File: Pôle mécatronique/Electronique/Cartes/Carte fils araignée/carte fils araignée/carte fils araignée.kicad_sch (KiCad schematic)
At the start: 17 parts, among them J1 Conn_01x05, J10 Conn_01x05, J11 Conn_01x05, J12 Conn_01x05, J13 Conn_01x05, J2 Conn_01x05, J3 Conn_01x05, J4 Conn_01x05, J5 Conn_01x03, J6 Conn_01x03, J7 Conn_01x05, J8 Conn_01x03, J9 Conn_01x04

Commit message: Update Araignée & Odométrie
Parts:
- J5: value Conn_01x03 -> X3
- J6: value Conn_01x03 -> X1
- J8: value Conn_01x03 -> X2
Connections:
- net Xshut5: now also J6.1 (Pin_1); no longer J6.2 (Pin_2)
- net Xshut6: now also J6.2 (Pin_2); no longer J6.1 (Pin_1)
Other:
- moved on the sheet: J5, J6, J8

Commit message: Panique totale
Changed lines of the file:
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@@
     (pin "4")
+  )
+  (symbol (lib_id "Graphic:Logo_Open_Hardware_Small") (at 238.76 48.26 0) (unit 1)
+    (in_bom yes) (on_board yes)
+    (property "Reference" "#LOGO1" (id 0) (at 238.76 41.275 0)
+      (effects (font (size 1.27 1.27)) hide)
+    )
+    (property "Value" "Logo_Open_Hardware_Small" (id 1) (at 238.76 53.975 0)
+      (effects (font (size 1.27 1.27)) hide)
+    )
+    (property "Footprint" "Logos:logoRobotechNancy10x10" (id 2) (at 238.76 48.26 0)
+      (effects (font (size 1.27 1.27)) hide)
+    )
+    (property "Datasheet" "~" (id 3) (at 238.76 48.26 0)
+      (effects (font (size 1.27 1.27)) hide)
+    )
   )
   (symbol (lib_id "Connector_Generic:Conn_01x05") (at 154.94 91.44 0) (mirror x) (unit 1)
@@
   )
   (symbol_instances
+    (path "/a543a4a0-b8e2-45a4-be48-7207020a5b1f"
+      (reference "#LOGO1") (unit 1) (value "Logo_Open_Hardware_Small") (footprint "Logos:logoRobotechNancy10x10")
+    )
     (path "/edcfc43d-85e7-4514-91a8-390c9edc311f"
       (reference "#PWR0101") (unit 1) (value "GND") (footprint "")

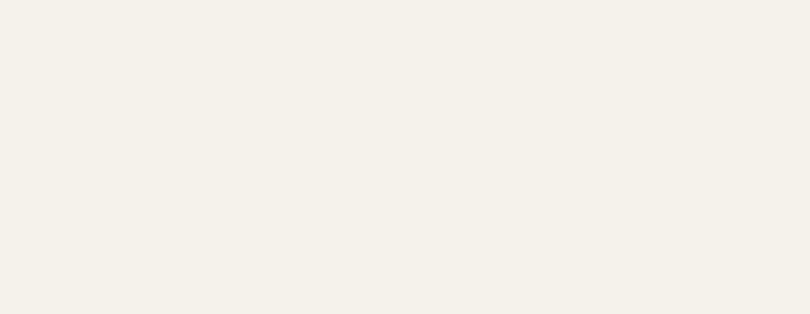
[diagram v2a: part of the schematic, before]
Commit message: Correction carte araignée
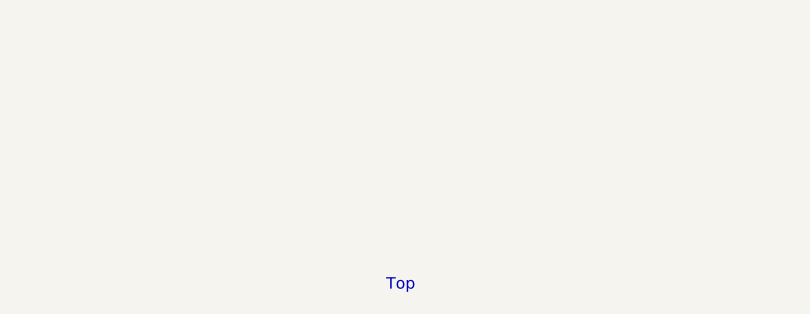
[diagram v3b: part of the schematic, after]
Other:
- note added: "Top"
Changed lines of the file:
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@@
     (stroke (width 0) (type default) (color 0 0 0 0))
+  )
+  (text "Top" (at 185.42 172.72 0)
+    (effects (font (size 1.27 1.27)) (justify left bottom))
   )
   (global_label "I2C_SCL" (shape input) (at 144.78 74.93 180) (fields_autoplaced)

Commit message: Version finale JLCPCB
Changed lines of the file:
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@@
       (effects (font (size 1.27 1.27)) (justify right))
     )
-    (property "Value" "X2" (id 1) (at 109.22 35.56 90)
+    (property "Value" "X2" (id 1) (at 110.49 36.83 90)
       (effects (font (size 1.27 1.27)) (justify right))
     )
